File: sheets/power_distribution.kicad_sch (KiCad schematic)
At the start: 5 parts

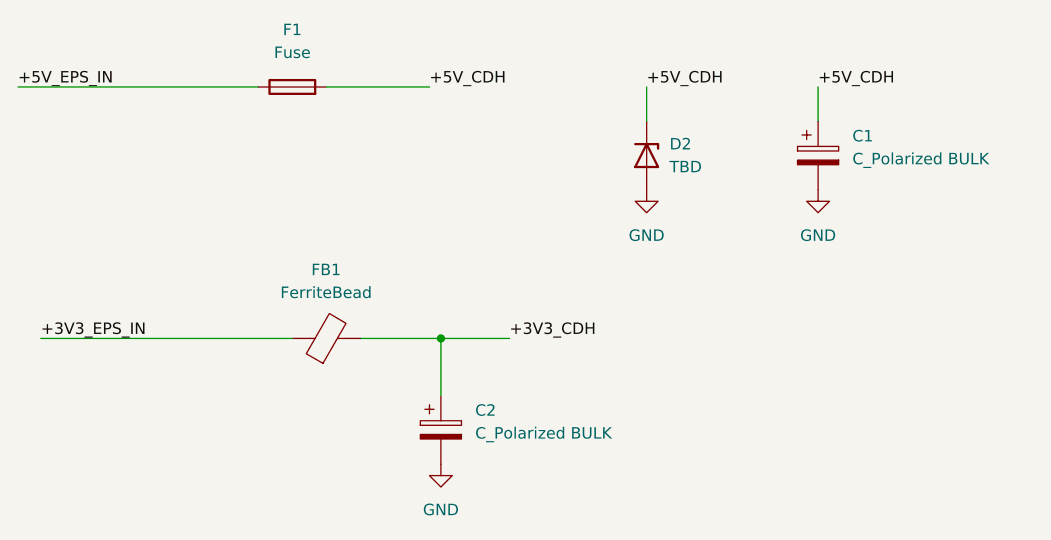
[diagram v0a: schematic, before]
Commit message: Merge Payload and thermals
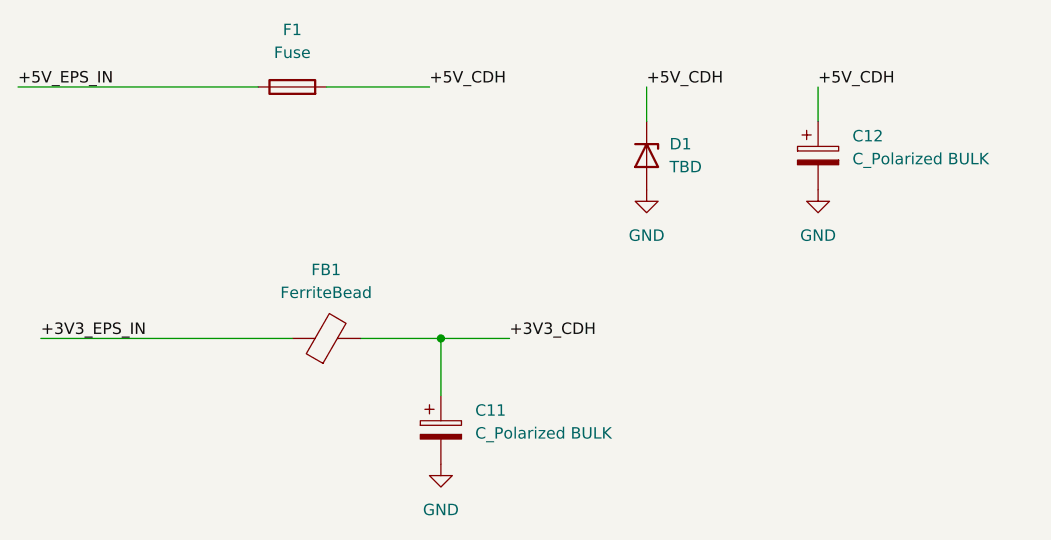
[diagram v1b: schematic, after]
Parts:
- renumbered C2 to C11, C1 to C12, D2 to D1
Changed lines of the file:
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@@
 		(dnp no)
 		(fields_autoplaced yes)
-		(property "Reference" "D2"
+		(property "Reference" "D1"
 			(at 130.81 72.3899 90)
 			(show_name no)
@@
 			(project "hs2-cdh-pcb"
 				(path "/e63e39d7-6ac0-4ffd-8aa3-1841a4541b55/197a3ee6-82d6-4332-9a6e-f9d2e34511e3"
-					(reference "D2")
+					(reference "D1")
 					(unit 1)
 				)
@@
 		(dnp no)
 		(fields_autoplaced yes)
-		(property "Reference" "#PWR02"
+		(property "Reference" "#PWR051"
 			(at 147.32 83.82 0)
 			(hide yes)
@@
 			(project "hs2-cdh-pcb"
 				(path "/e63e39d7-6ac0-4ffd-8aa3-1841a4541b55/197a3ee6-82d6-4332-9a6e-f9d2e34511e3"
-					(reference "#PWR02")
+					(reference "#PWR051")
 					(unit 1)
 				)
@@
 		(dnp no)
 		(fields_autoplaced yes)
-		(property "Reference" "#PWR03"
+		(property "Reference" "#PWR049"
 			(at 105.41 114.3 0)
 			(hide yes)
@@
 			(project "hs2-cdh-pcb"
 				(path "/e63e39d7-6ac0-4ffd-8aa3-1841a4541b55/197a3ee6-82d6-4332-9a6e-f9d2e34511e3"
-					(reference "#PWR03")
+					(reference "#PWR049")
 					(unit 1)
 				)
@@
 		(dnp no)
 		(fields_autoplaced yes)
-		(property "Reference" "#PWR04"
+		(property "Reference" "#PWR050"
 			(at 128.27 83.82 0)
 			(hide yes)
@@
 			(project "hs2-cdh-pcb"
 				(path "/e63e39d7-6ac0-4ffd-8aa3-1841a4541b55/197a3ee6-82d6-4332-9a6e-f9d2e34511e3"
-					(reference "#PWR04")
+					(reference "#PWR050")
 					(unit 1)
 				)
@@
 		(dnp no)
 		(fields_autoplaced yes)
-		(property "Reference" "C1"
+		(property "Reference" "C12"
 			(at 151.13 71.5009 0)
 			(show_name no)
@@
 			(project "hs2-cdh-pcb"
 				(path "/e63e39d7-6ac0-4ffd-8aa3-1841a4541b55/197a3ee6-82d6-4332-9a6e-f9d2e34511e3"
-					(reference "C1")
+					(reference "C12")
 					(unit 1)
 				)
@@
 		(dnp no)
 		(fields_autoplaced yes)
-		(property "Reference" "C2"
+		(property "Reference" "C11"
 			(at 109.22 101.9809 0)
 			(show_name no)
@@
 			(project "hs2-cdh-pcb"
 				(path "/e63e39d7-6ac0-4ffd-8aa3-1841a4541b55/197a3ee6-82d6-4332-9a6e-f9d2e34511e3"
-					(reference "C2")
-					(unit 1)
-				)
+					(reference "C11")
+					(unit 1)
+				)
